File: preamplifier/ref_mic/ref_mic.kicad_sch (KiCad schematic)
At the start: 44 parts, among them J1 MEMS micbias, J2 Mini XLR Male, U1 OPA1664

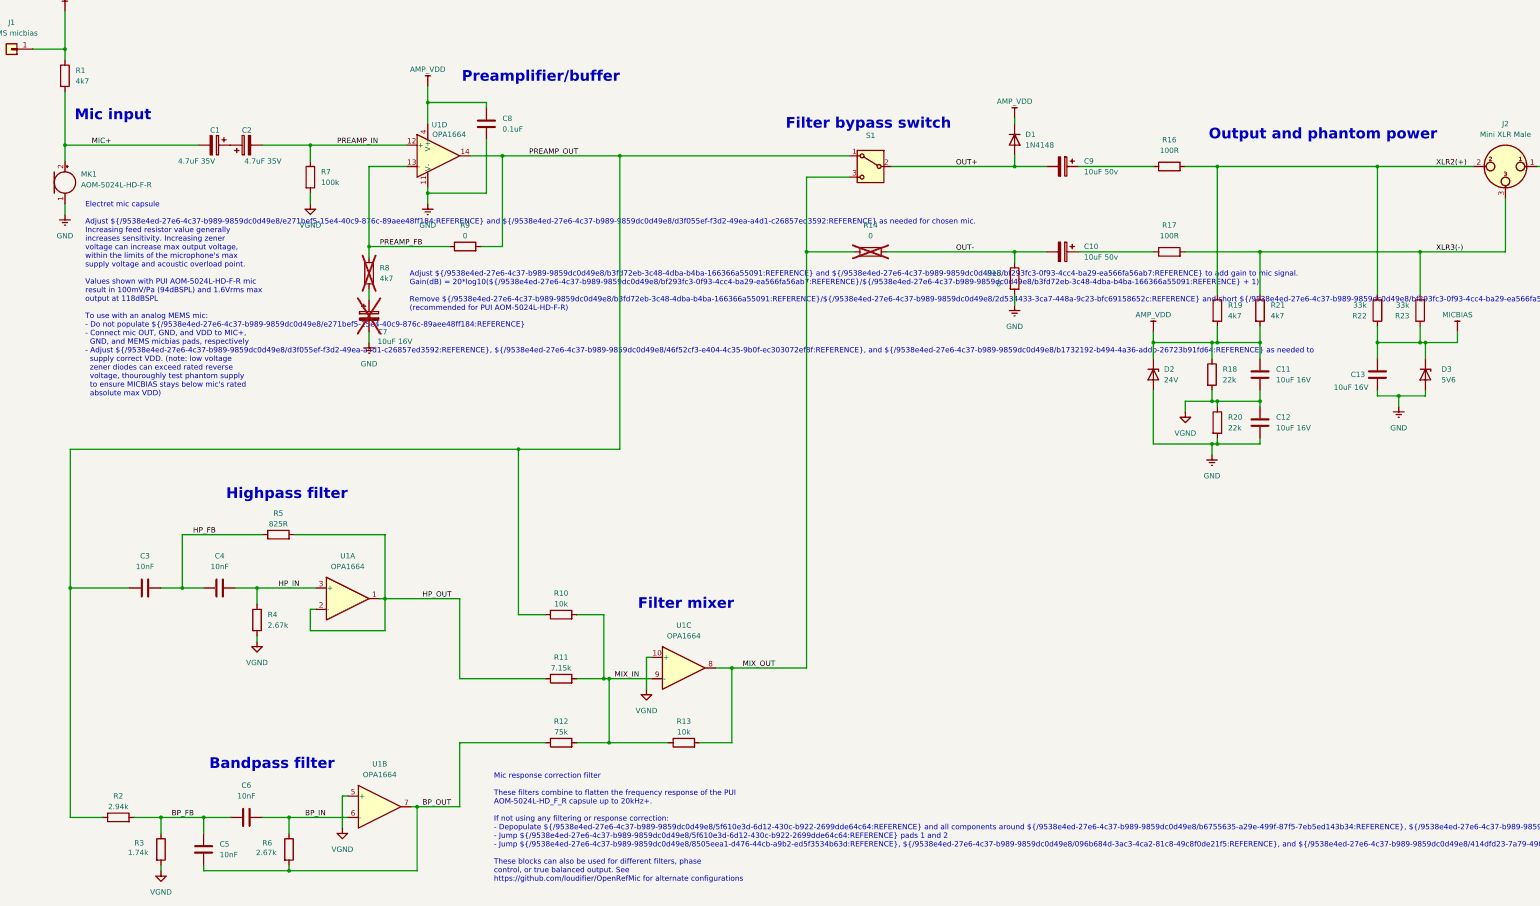
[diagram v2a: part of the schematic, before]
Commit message: major v2 updates
fixes based on initial v2 PCB build
- R6 corrected to 8.06k
- Replaced opamp with OPA4991
- Adjust phantom power resistor values to optimize opamp Vdd
- Connect R15 to VGND to avoid exceeding C10 voltage rating
- Increase values of input AC-coupling caps, output caps, phantom power caps, decrease output series resistors. Reduces low frequency rolloff
- Add D4 for alternate configs where In- is connected to an opamp output
- Improved PCB layout
- Improved CAD design, add soldering jig
- Add 3MF with print settings for grille and body

Update preamp documentation, add instructions for no/alternate filtering configs
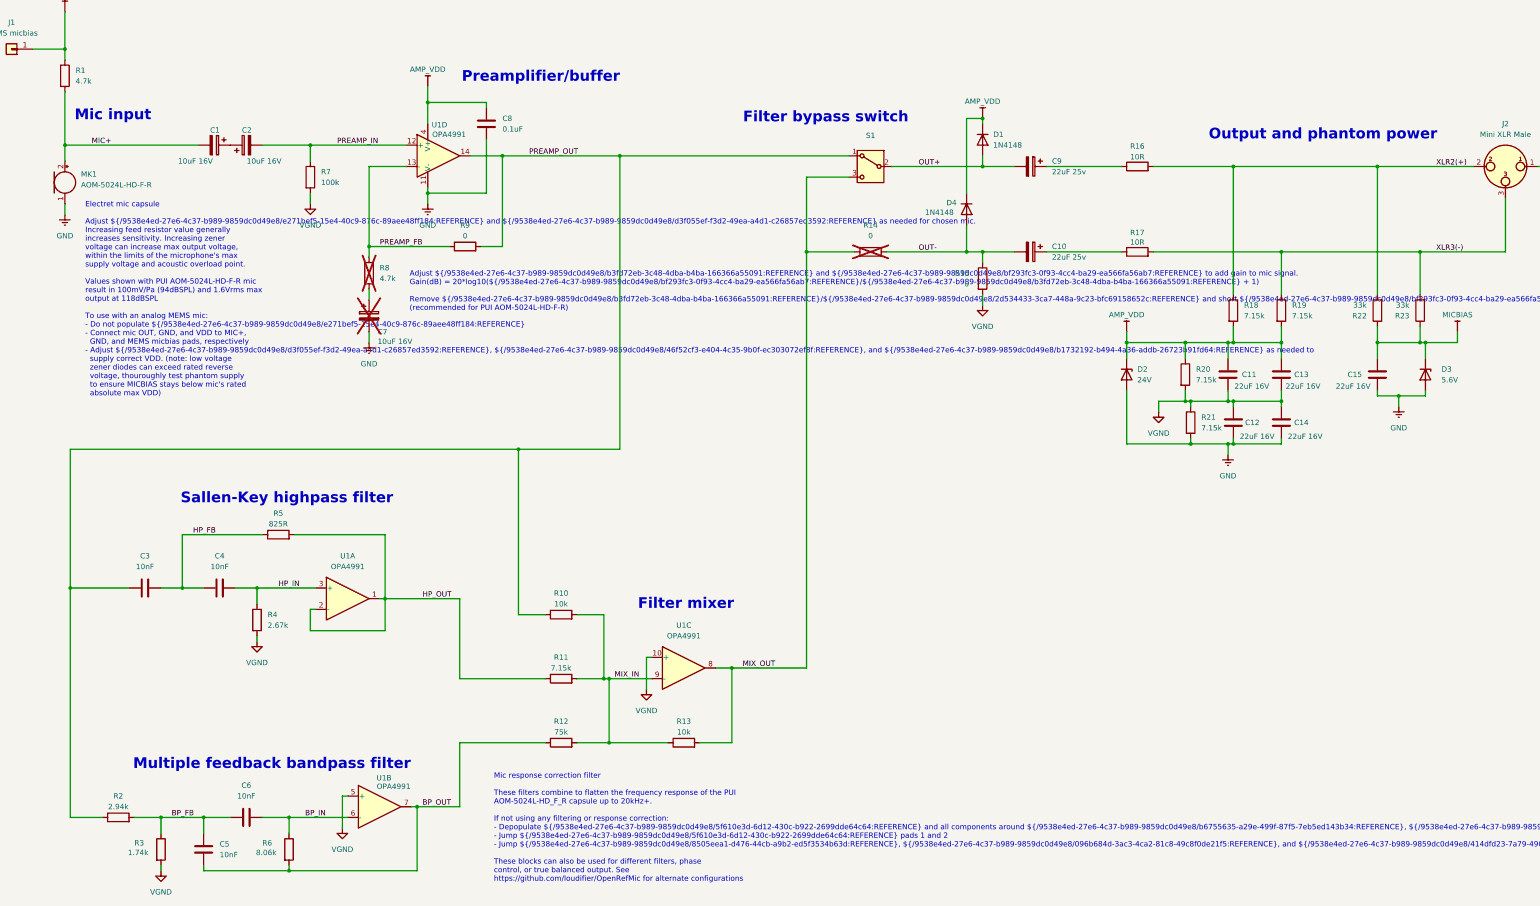
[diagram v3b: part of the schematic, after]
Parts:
- added C13, C14: 22uF 16V, OpenRefMic:C_1210_3225Metric_0.95mm-height, symbol Device:C
- added D4: 1N4148, Diode_SMD:D_SOD-523, symbol Device:D
- C1, C2: value 4.7uF 35V -> 10uF 16V; DigiKey_Part_Number UZR1V4R7MCL1GB -> UZG1C100MCL1GB
- C10, C9: value 10uF 50v -> 22uF 25v; DigiKey_Part_Number UZG1H100MCL1GB -> UZG1E220MCL1GB; LCSC_Part_Number Honor Elec GVS1H100M0604 -> Nichicon UZG1E220MCL1GB
- C11, C12: value 10uF 16V -> 22uF 16V; footprint Capacitor_SMD:C_1206_3216Metric -> OpenRefMic:C_1210_3225Metric_0.95mm-height; DigiKey_Part_Number CL31B106KOHNNNE -> EMK325BJ226MD-T; LCSC_Part_Number Samsung Electro-Mechanics CL31B106KOHNNNE -> Taiyo Yuden EMK325BJ226MD-T
- C15: renamed from C13; value 10uF 16V -> 22uF 16V; footprint Capacitor_SMD:C_1206_3216Metric -> OpenRefMic:C_1210_3225Metric_0.95mm-height; DigiKey_Part_Number CL31B106KOHNNNE -> EMK325BJ226MD-T; LCSC_Part_Number Samsung Electro-Mechanics CL31B106KOHNNNE -> Taiyo Yuden EMK325BJ226MD-T
- D3: value 5V6 -> 5.6V
- J1: footprint Connector_PinHeader_2.54mm:PinHeader_1x01_P2.54mm_Vertical -> Connector_Wire:SolderWire-0.1sqmm_1x01_D0.4mm_OD1mm
- R1, R8: value 4k7 -> 4.7k
- R16, R17: value 100R -> 10R; DigiKey_Part_Number RC0402FR-07100RL -> RC0402FR-0710RL; LCSC_Part_Number YAGEO RC0402FR-07100RL -> YAGEO RC0402FR-0710RL
- R18: renamed from R19; value 4k7 -> 7.15k; DigiKey_Part_Number RC0402FR-074K7L -> RC0402FR-077K15L; LCSC_Part_Number YAGEO RC0402FR-074K7L -> YAGEO RC0402FR-077K15L
- R19: renamed from R21; value 4k7 -> 7.15k; DigiKey_Part_Number RC0402FR-074K7L -> RC0402FR-077K15L; LCSC_Part_Number YAGEO RC0402FR-074K7L -> YAGEO RC0402FR-077K15L
- R20: renamed from R18; value 22k -> 7.15k; DigiKey_Part_Number RC0402FR-0722KL -> RC0402FR-077K15L; LCSC_Part_Number YAGEO RC0402FR-0722KL -> YAGEO RC0402FR-077K15L
- R21: renamed from R20; value 22k -> 7.15k; DigiKey_Part_Number RC0402FR-0722KL -> RC0402FR-077K15L; LCSC_Part_Number YAGEO RC0402FR-0722KL -> YAGEO RC0402FR-077K15L
- R6: value 2.67k -> 8.06k; DigiKey_Part_Number RC0402FR-072K67L -> RC0402FR-138K06L; LCSC_Part_Number YAGEO RC0402FR-072K67L -> YAGEO AC0402FR-078K06L
- U1: value OPA1664 -> OPA4991; DigiKey_Part_Number OPA1664AIDR -> OPA4991IDR; LCSC_Part_Number TI OPA1664AID -> TI OPA4991IDR
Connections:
- net AMP_VDD: now also C13.1, D4.1 (K)
- net GND: now also C14.2; no longer R15.2
- net OUT-: now also D4.2 (A)
- net VGND: now also R15.2, C13.2, C14.1
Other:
- note added: "Multiple feedback bandpass filter"
- note added: "Sallen-Key highpass filter"
- note removed: "Bandpass filter"
- note removed: "Highpass filter"
- moved on the sheet: C10, C11, C12, C9, D1, D2, R15, R16, R17, R18, R19, R20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

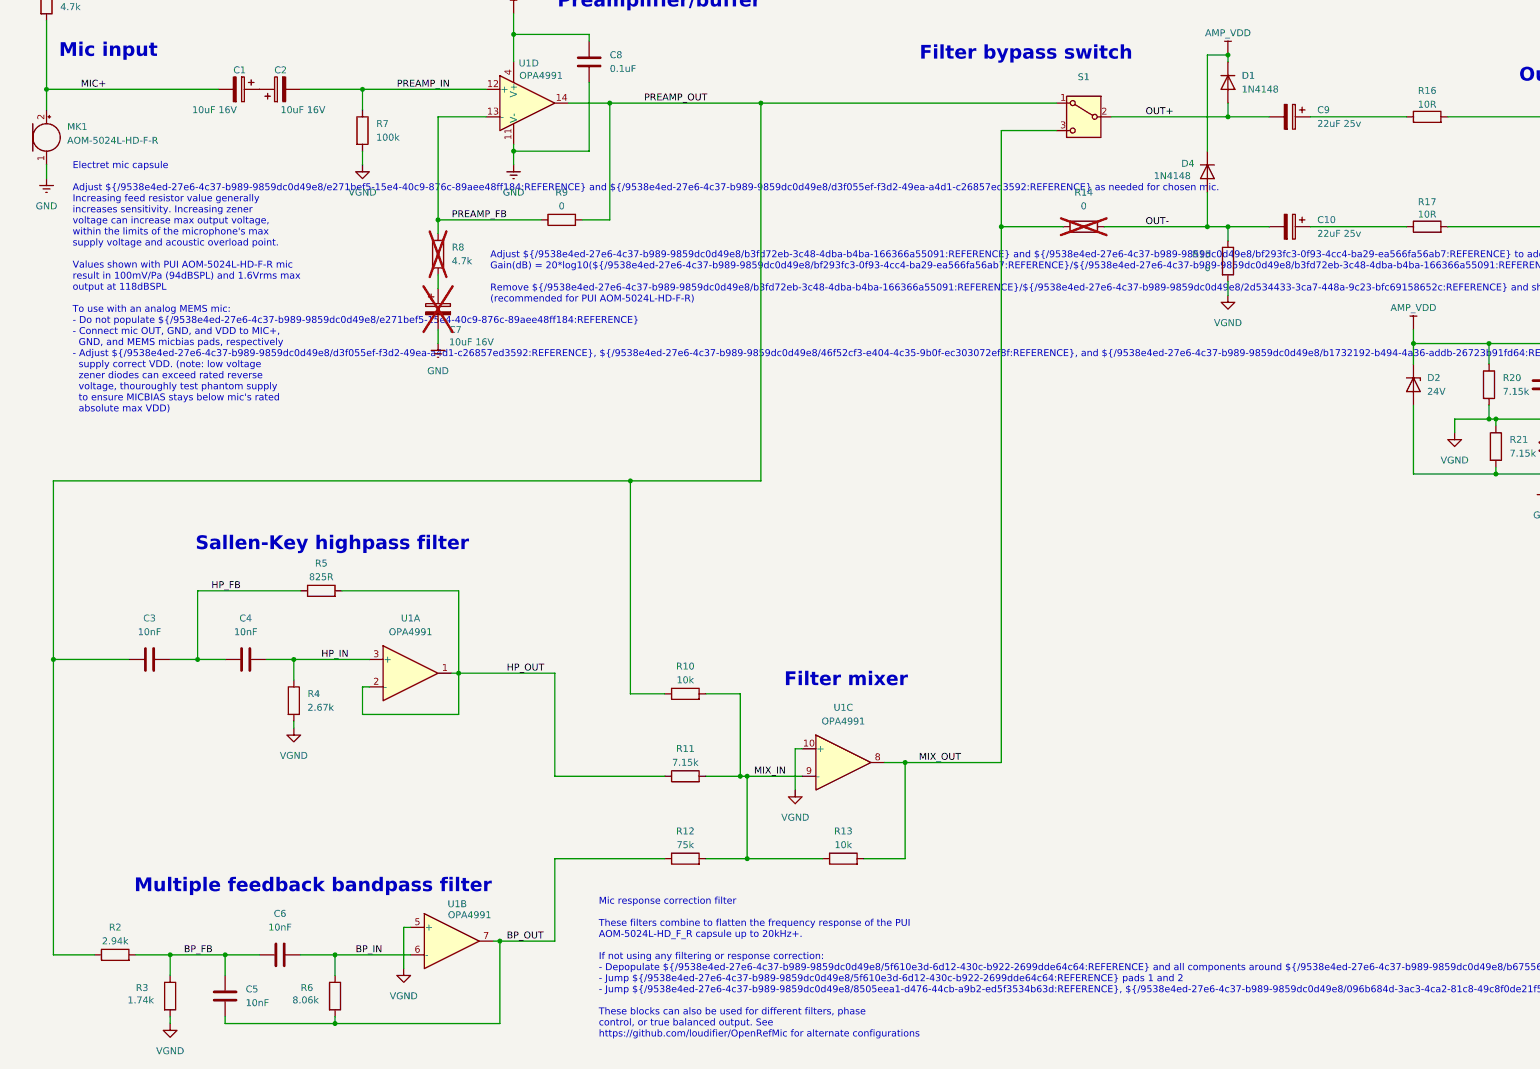
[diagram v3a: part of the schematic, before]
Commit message: major v2 updates
Likely the final versions of v2 design files
- updated CAD. Small tweaks to spacers, modeled in grille openings (instead of relying on slicer settings), increased room for taller caps, increased clearance for header pins on bottom of PCB
- Updated EQ component values based on measurements of several prototypes (original v1 prototype capsule response deviated significantly from other 5+ other capsules tested).
- Added PCB thickness requirement note to preamp doc and directly on fab layer of layout
- Updated all KiCAD files, gerber outputs, schematic outputs, etc.
- updated readme, preamp docs
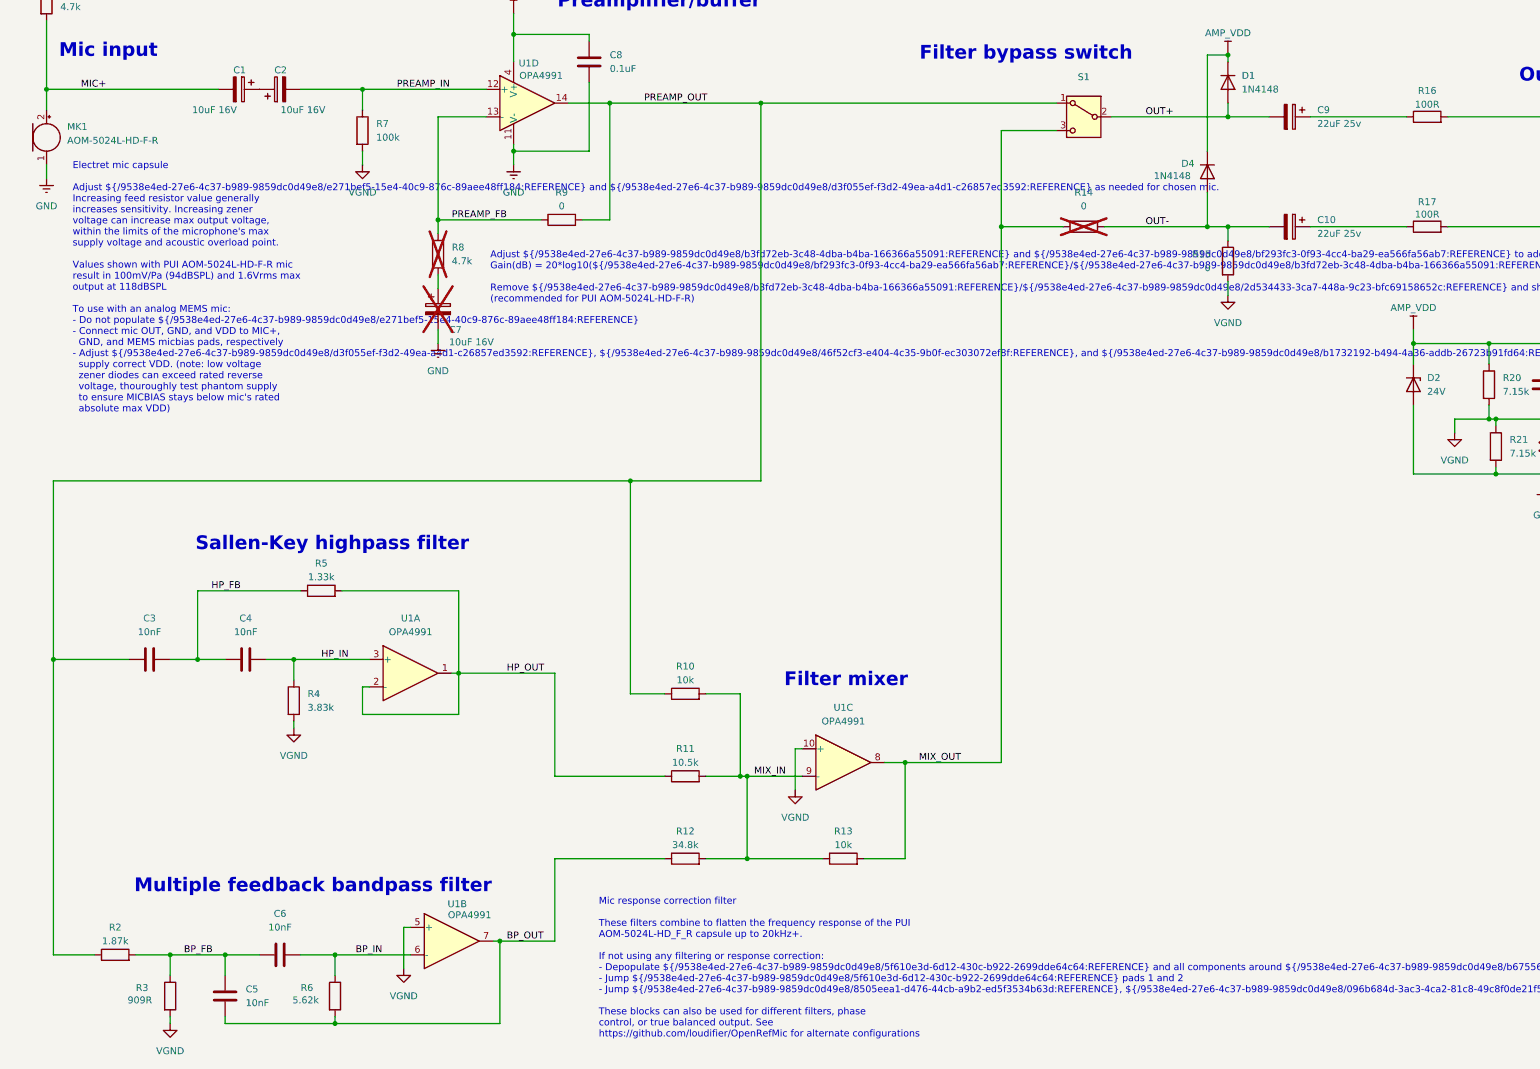
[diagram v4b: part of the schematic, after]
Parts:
- R11: value 7.15k -> 10.5k; DigiKey_Part_Number RC0402FR-077K15L -> RC0402FR-0710K5L; LCSC_Part_Number YAGEO RC0402FR-077K15L -> YAGEO RC0402FR-0710K5L
- R12: value 75k -> 34.8k; DigiKey_Part_Number RC0402FR-1375KL -> RC0402FR-0734K8L; LCSC_Part_Number YAGEO RC0402FR-1375KL -> YAGEO RC0402FR-0734K8L
- R16, R17: value 10R -> 100R; DigiKey_Part_Number RC0402FR-0710RL -> RC0402FR-07100RL; LCSC_Part_Number YAGEO RC0402FR-0710RL -> YAGEO RC0402FR-07100RL
- R2: value 2.94k -> 1.87k; DigiKey_Part_Number RC0402FR-072K94L -> RC0402FR-131K87L; LCSC_Part_Number YAGEO RC0402FR-072K94L -> YAGEO RC0402FR-131K87L
- R3: value 1.74k -> 909R; DigiKey_Part_Number RC0402FR-071K74L -> RC0402FR-07909RL; LCSC_Part_Number YAGEO RC0402FR-071K74L -> YAGEO RC0402FR-07909RL
- R4: value 2.67k -> 3.83k; DigiKey_Part_Number RC0402FR-072K67L -> RC0402FR-073K83L; LCSC_Part_Number YAGEO RC0402FR-072K67L -> YAGEO RC0402FR-073K83L
- R5: value 825R -> 1.33k; DigiKey_Part_Number RC0402FR-07825RL -> RC0402FR-131K33L; LCSC_Part_Number YAGEO RC0402FR-07825RL -> YAGEO RC0402FR-131K33L
- R6: value 8.06k -> 5.62k; DigiKey_Part_Number RC0402FR-138K06L -> RC0402FR-075K62L; LCSC_Part_Number YAGEO AC0402FR-078K06L -> YAGEO RC0402FR-075K62L
